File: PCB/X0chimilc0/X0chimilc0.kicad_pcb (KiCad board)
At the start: 2 copper layers, 12 parts, among them J1 Conn_02x12_Odd_Even, T1 SDS-50J, T12 ACJS-MHDR, T13 ACJS-MHDR, T14 ACJS-MHDR, T15 ACJS-MHDR, T16 ACJS-MHDR, T2 SDS-50J, T3 SDS-50J, U1 STM32H745XIH6, U2 ECP5UM5G_85_CABGA381, U3 WM8994ECS-R

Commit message: Memory Datatsheet
Memory datasheet added
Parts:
- moved U3 51.5 mm to (160.3, 83.2)
- moved J1 43.1 mm to (238.0, 99.5), turned to 90 degrees
- moved U1 19.3 mm to (180.1, 83.8)
- moved T14 14.8 mm to (118.3, 60.9)
- moved T16 14.8 mm to (135.6, 60.9)
- moved U2 14.4 mm to (217.4, 86.0)
- moved T1 9.55 mm to (239.6, 56.9)
- moved T2 9.55 mm to (189.6, 57.0)
- moved T3 9.55 mm to (211.1, 57.1)
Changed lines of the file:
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@@
   )
   (module Connectors_Harwin:Harwin_LTek-Male_2x13x2.00mm_Straight_StrainRelief (layer F.Cu)
-    (at 197.55 114.5)
+    (at 238 99.5 90)
     (descr "Harwin LTek Connector, 26 pins, single row male, vertical entry, strain relief clip")
     (tags "connector harwin ltek M80")
-    (fp_text reference J1 (at 12 -5.5) (layer F.SilkS)
-      (effects (font (size 1 1) (thickness 0.15)))
-    )
-    (fp_text value Conn_02x12_Odd_Even (at 12 4) (layer F.Fab)
-      (effects (font (size 1 1) (thickness 0.15)))
-    )
-    (fp_text user %R (at 12 -1) (layer F.Fab)
+    (fp_text reference J1 (at 12 -5.5 90) (layer F.SilkS)
+      (effects (font (size 1 1) (thickness 0.15)))
+    )
+    (fp_text value Conn_02x12_Odd_Even (at 12 4 90) (layer F.Fab)
+      (effects (font (size 1 1) (thickness 0.15)))
+    )
+    (fp_text user %R (at 12 -1 90) (layer F.Fab)
       (effects (font (size 1 1) (thickness 0.15)))
     )
@@
     (fp_line (start -0.3 3.1) (end 0.3 3.1) (layer F.Fab) (width 0.1))
     (fp_line (start 0.3 3.1) (end 0 2.5) (layer F.Fab) (width 0.1))
-    (pad 1 thru_hole rect (at 0 0) (size 1.35 1.35) (drill 0.8) (layers *.Cu *.Mask)
+    (pad 1 thru_hole rect (at 0 0 90) (size 1.35 1.35) (drill 0.8) (layers *.Cu *.Mask)
       (net 757 "Net-(J1-Pad1)"))
-    (pad 2 thru_hole circle (at 2 0) (size 1.35 1.35) (drill 0.8) (layers *.Cu *.Mask)
+    (pad 2 thru_hole circle (at 2 0 90) (size 1.35 1.35) (drill 0.8) (layers *.Cu *.Mask)
       (net 758 "Net-(J1-Pad2)"))
-    (pad 3 thru_hole circle (at 4 0) (size 1.35 1.35) (drill 0.8) (layers *.Cu *.Mask)
+    (pad 3 thru_hole circle (at 4 0 90) (size 1.35 1.35) (drill 0.8) (layers *.Cu *.Mask)
       (net 759 "Net-(J1-Pad3)"))
-    (pad 4 thru_hole circle (at 6 0) (size 1.35 1.35) (drill 0.8) (layers *.Cu *.Mask)
+    (pad 4 thru_hole circle (at 6 0 90) (size 1.35 1.35) (drill 0.8) (layers *.Cu *.Mask)
       (net 760 "Net-(J1-Pad4)"))
-    (pad 5 thru_hole circle (at 8 0) (size 1.35 1.35) (drill 0.8) (layers *.Cu *.Mask)
+    (pad 5 thru_hole circle (at 8 0 90) (size 1.35 1.35) (drill 0.8) (layers *.Cu *.Mask)
       (net 761 "Net-(J1-Pad5)"))
-    (pad 6 thru_hole circle (at 10 0) (size 1.35 1.35) (drill 0.8) (layers *.Cu *.Mask)
+    (pad 6 thru_hole circle (at 10 0 90) (size 1.35 1.35) (drill 0.8) (layers *.Cu *.Mask)
       (net 762 "Net-(J1-Pad6)"))
-    (pad 7 thru_hole circle (at 12 0) (size 1.35 1.35) (drill 0.8) (layers *.Cu *.Mask)
+    (pad 7 thru_hole circle (at 12 0 90) (size 1.35 1.35) (drill 0.8) (layers *.Cu *.Mask)
       (net 763 "Net-(J1-Pad7)"))
-    (pad 8 thru_hole circle (at 14 0) (size 1.35 1.35) (drill 0.8) (layers *.Cu *.Mask)
+    (pad 8 thru_hole circle (at 14 0 90) (size 1.35 1.35) (drill 0.8) (layers *.Cu *.Mask)
       (net 764 "Net-(J1-Pad8)"))
-    (pad 9 thru_hole circle (at 16 0) (size 1.35 1.35) (drill 0.8) (layers *.Cu *.Mask)
+    (pad 9 thru_hole circle (at 16 0 90) (size 1.35 1.35) (drill 0.8) (layers *.Cu *.Mask)
       (net 765 "Net-(J1-Pad9)"))
-    (pad 10 thru_hole circle (at 18 0) (size 1.35 1.35) (drill 0.8) (layers *.Cu *.Mask)
+    (pad 10 thru_hole circle (at 18 0 90) (size 1.35 1.35) (drill 0.8) (layers *.Cu *.Mask)
       (net 766 "Net-(J1-Pad10)"))
-    (pad 11 thru_hole circle (at 20 0) (size 1.35 1.35) (drill 0.8) (layers *.Cu *.Mask)
+    (pad 11 thru_hole circle (at 20 0 90) (size 1.35 1.35) (drill 0.8) (layers *.Cu *.Mask)
       (net 767 "Net-(J1-Pad11)"))
-    (pad 12 thru_hole circle (at 22 0) (size 1.35 1.35) (drill 0.8) (layers *.Cu *.Mask)
+    (pad 12 thru_hole circle (at 22 0 90) (size 1.35 1.35) (drill 0.8) (layers *.Cu *.Mask)
       (net 768 "Net-(J1-Pad12)"))
-    (pad 13 thru_hole circle (at 24 0) (size 1.35 1.35) (drill 0.8) (layers *.Cu *.Mask)
+    (pad 13 thru_hole circle (at 24 0 90) (size 1.35 1.35) (drill 0.8) (layers *.Cu *.Mask)
       (net 769 "Net-(J1-Pad13)"))
-    (pad 14 thru_hole circle (at 0 -2) (size 1.35 1.35) (drill 0.8) (layers *.Cu *.Mask)
+    (pad 14 thru_hole circle (at 0 -2 90) (size 1.35 1.35) (drill 0.8) (layers *.Cu *.Mask)
       (net 770 "Net-(J1-Pad14)"))
-    (pad 15 thru_hole circle (at 2 -2) (size 1.35 1.35) (drill 0.8) (layers *.Cu *.Mask)
+    (pad 15 thru_hole circle (at 2 -2 90) (size 1.35 1.35) (drill 0.8) (layers *.Cu *.Mask)
       (net 771 "Net-(J1-Pad15)"))
-    (pad 16 thru_hole circle (at 4 -2) (size 1.35 1.35) (drill 0.8) (layers *.Cu *.Mask)
+    (pad 16 thru_hole circle (at 4 -2 90) (size 1.35 1.35) (drill 0.8) (layers *.Cu *.Mask)
       (net 772 "Net-(J1-Pad16)"))
-    (pad 17 thru_hole circle (at 6 -2) (size 1.35 1.35) (drill 0.8) (layers *.Cu *.Mask)
+    (pad 17 thru_hole circle (at 6 -2 90) (size 1.35 1.35) (drill 0.8) (layers *.Cu *.Mask)
       (net 773 "Net-(J1-Pad17)"))
-    (pad 18 thru_hole circle (at 8 -2) (size 1.35 1.35) (drill 0.8) (layers *.Cu *.Mask)
+    (pad 18 thru_hole circle (at 8 -2 90) (size 1.35 1.35) (drill 0.8) (layers *.Cu *.Mask)
       (net 774 "Net-(J1-Pad18)"))
-    (pad 19 thru_hole circle (at 10 -2) (size 1.35 1.35) (drill 0.8) (layers *.Cu *.Mask)
+    (pad 19 thru_hole circle (at 10 -2 90) (size 1.35 1.35) (drill 0.8) (layers *.Cu *.Mask)
       (net 775 "Net-(J1-Pad19)"))
-    (pad 20 thru_hole circle (at 12 -2) (size 1.35 1.35) (drill 0.8) (layers *.Cu *.Mask)
+    (pad 20 thru_hole circle (at 12 -2 90) (size 1.35 1.35) (drill 0.8) (layers *.Cu *.Mask)
       (net 776 "Net-(J1-Pad20)"))
-    (pad 21 thru_hole circle (at 14 -2) (size 1.35 1.35) (drill 0.8) (layers *.Cu *.Mask)
+    (pad 21 thru_hole circle (at 14 -2 90) (size 1.35 1.35) (drill 0.8) (layers *.Cu *.Mask)
       (net 777 "Net-(J1-Pad21)"))
-    (pad 22 thru_hole circle (at 16 -2) (size 1.35 1.35) (drill 0.8) (layers *.Cu *.Mask)
+    (pad 22 thru_hole circle (at 16 -2 90) (size 1.35 1.35) (drill 0.8) (layers *.Cu *.Mask)
       (net 778 "Net-(J1-Pad22)"))
-    (pad 23 thru_hole circle (at 18 -2) (size 1.35 1.35) (drill 0.8) (layers *.Cu *.Mask)
+    (pad 23 thru_hole circle (at 18 -2 90) (size 1.35 1.35) (drill 0.8) (layers *.Cu *.Mask)
       (net 779 "Net-(J1-Pad23)"))
-    (pad 24 thru_hole circle (at 20 -2) (size 1.35 1.35) (drill 0.8) (layers *.Cu *.Mask)
+    (pad 24 thru_hole circle (at 20 -2 90) (size 1.35 1.35) (drill 0.8) (layers *.Cu *.Mask)
       (net 780 "Net-(J1-Pad24)"))
-    (pad 25 thru_hole circle (at 22 -2) (size 1.35 1.35) (drill 0.8) (layers *.Cu *.Mask))
-    (pad 26 thru_hole circle (at 24 -2) (size 1.35 1.35) (drill 0.8) (layers *.Cu *.Mask))
-    (pad "" np_thru_hole circle (at -2.25 -3.375) (size 0.95 0.95) (drill 0.95) (layers *.Cu *.Mask))
-    (pad "" np_thru_hole circle (at -2.25 1.375) (size 0.95 0.95) (drill 0.95) (layers *.Cu *.Mask))
-    (pad "" np_thru_hole circle (at 26.25 -3.375) (size 0.95 0.95) (drill 0.95) (layers *.Cu *.Mask))
-    (pad "" np_thru_hole circle (at 26.25 1.375) (size 0.95 0.95) (drill 0.95) (layers *.Cu *.Mask))
+    (pad 25 thru_hole circle (at 22 -2 90) (size 1.35 1.35) (drill 0.8) (layers *.Cu *.Mask))
+    (pad 26 thru_hole circle (at 24 -2 90) (size 1.35 1.35) (drill 0.8) (layers *.Cu *.Mask))
+    (pad "" np_thru_hole circle (at -2.25 -3.375 90) (size 0.95 0.95) (drill 0.95) (layers *.Cu *.Mask))
+    (pad "" np_thru_hole circle (at -2.25 1.375 90) (size 0.95 0.95) (drill 0.95) (layers *.Cu *.Mask))
+    (pad "" np_thru_hole circle (at 26.25 -3.375 90) (size 0.95 0.95) (drill 0.95) (layers *.Cu *.Mask))
+    (pad "" np_thru_hole circle (at 26.25 1.375 90) (size 0.95 0.95) (drill 0.95) (layers *.Cu *.Mask))
     (model ${KISYS3DMOD}/Connectors_Harwin.3dshapes/Harwin_LTek-Male_2x13x2.00mm_Straight_StrainRelief.wrl
       (at (xyz 0 0 0))
@@
   )
   (module AVR-KiCAD-Lib-ICs:WM8994ECS_R (layer F.Cu)
-    (at 109.2 77.15)
+    (at 160.3 83.15)
     (attr smd)
     (fp_text reference U3 (at 0 -3.0165) (layer F.SilkS)
@@
   )
   (module AVR-KiCAD-Lib-ICs:381caBGA_LATTICE (layer F.Cu)
-    (at 205.4 93.85)
+    (at 217.45 86)
     (attr smd)
     (fp_text reference U2 (at 0 -9.5) (layer F.SilkS)
@@
   )
   (module AVR-KiCAD-Lib-ICs:STM32H745XIH6 (layer F.Cu)
-    (at 161.7 89.75)
+    (at 180.1 83.85)
     (attr smd)
     (fp_text reference U1 (at 0 -8.075) (layer F.SilkS)
@@
   )
   (module AVR-KiCAD-Lib-Connectors:ACJS-MHDR (layer F.Cu)
-    (at 150.3 60.5 90)
+    (at 135.55 60.85 90)
     (fp_text reference T16 (at -10.15 -8.9 90) (layer F.SilkS)
       (effects (font (size 1 1) (thickness 0.15)))
@@
   )
   (module AVR-KiCAD-Lib-Connectors:ACJS-MHDR (layer F.Cu)
-    (at 133.1 60.5 90)
+    (at 118.35 60.85 90)
     (fp_text reference T14 (at -10.15 -8.9 90) (layer F.SilkS)
       (effects (font (size 1 1) (thickness 0.15)))
@@
   )
   (module AVR-KiCAD-Lib-ICs:SDS-50J (layer F.Cu)
-    (at 201.5 57.1 180)
+    (at 211.05 57.1 180)
     (fp_text reference T3 (at 0 0.5) (layer F.SilkS)
       (effects (font (size 1 1) (thickness 0.15)))
@@
   )
   (module AVR-KiCAD-Lib-ICs:SDS-50J (layer F.Cu)
-    (at 180 57 180)
+    (at 189.55 57 180)
     (fp_text reference T2 (at 0 0.5) (layer F.SilkS)
       (effects (font (size 1 1) (thickness 0.15)))
@@
   )
   (module AVR-KiCAD-Lib-ICs:SDS-50J (layer F.Cu)
-    (at 230 56.9 180)
+    (at 239.55 56.9 180)
     (fp_text reference T1 (at 0 0.5) (layer F.SilkS)
       (effects (font (size 1 1) (thickness 0.15)))

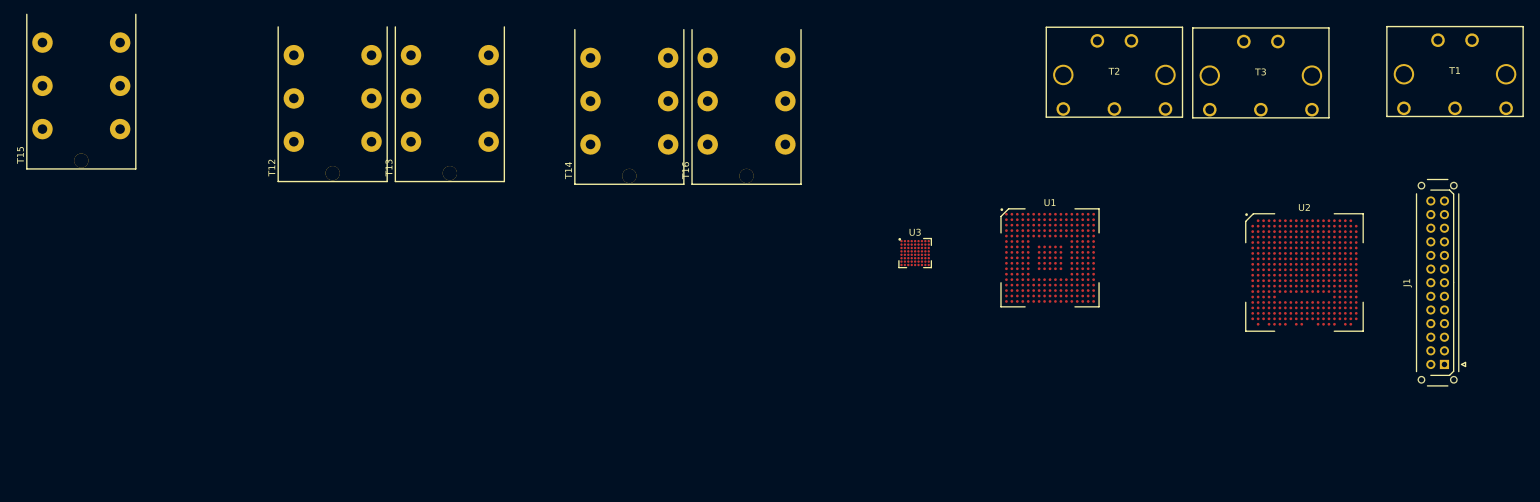
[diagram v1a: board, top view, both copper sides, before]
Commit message: Component PDFs
added relevant PDF datasheets and some minor schematic edits
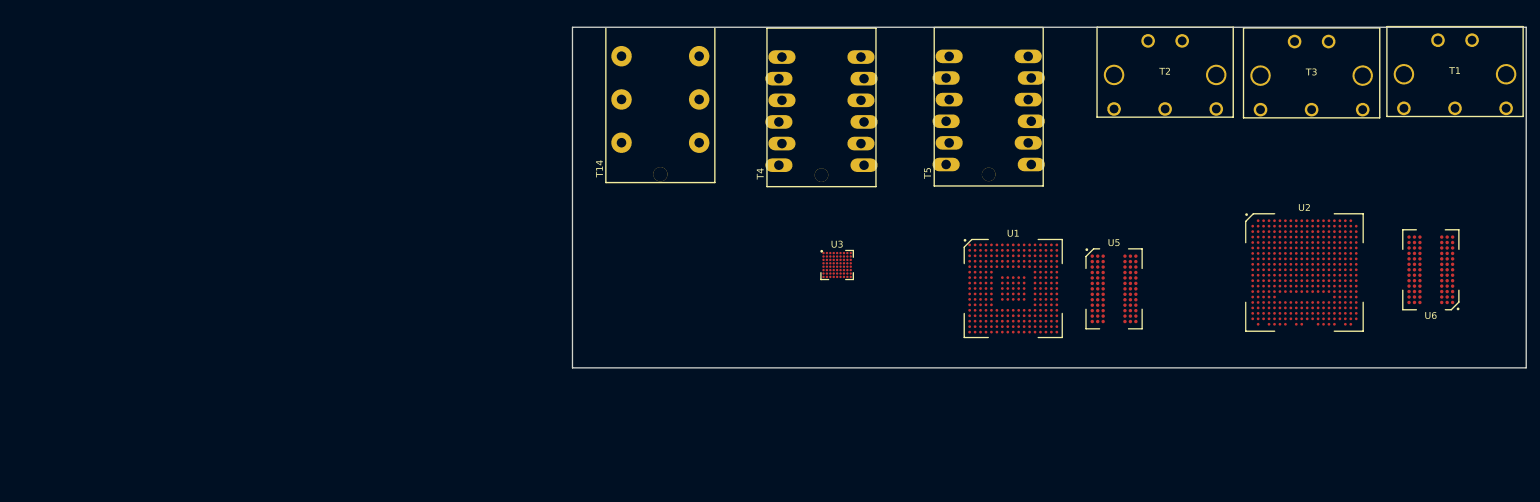
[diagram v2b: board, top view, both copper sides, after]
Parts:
- removed J1: Conn_02x12_Odd_Even, Connectors_Harwin:Harwin_LTek-Male_2x13x2.00mm_Straight_StrainRelief
- removed T12, T13, T15, T16: ACJS-MHDR, AVR-KiCAD-Lib-Connectors:ACJS-MHDR
- added T4: ACJS-MHDC, AVR-KiCAD-Lib-Connectors:ACJS-MHDC, F.Cu at (146.6, 63.9)
- added T5: ACJS-MHDC, AVR-KiCAD-Lib-Connectors:ACJS-MHDC, F.Cu at (171.1, 63.8)
- added U5: MT41K64M16TW-107_J-TR, AVR-KiCAD-Lib-ICs:MT41K64M16TW_107_J_TR, F.Cu at (189.5, 88.4)
- added U6: MT41K64M16TW-107_J-TR, AVR-KiCAD-Lib-ICs:MT41K64M16TW_107_J_TR, F.Cu at (236.0, 85.6)
- moved U3 11.6 mm to (148.8, 84.9)
- moved T2 7.45 mm to (197.0, 57.0)
- moved T3 7.45 mm to (218.5, 57.1)
- moved U1 7.03 mm to (174.7, 88.3)
- moved T14 4.56 mm to (122.9, 60.6)
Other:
- board outline added: 140 x 50 mm
